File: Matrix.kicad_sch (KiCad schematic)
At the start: 2 parts

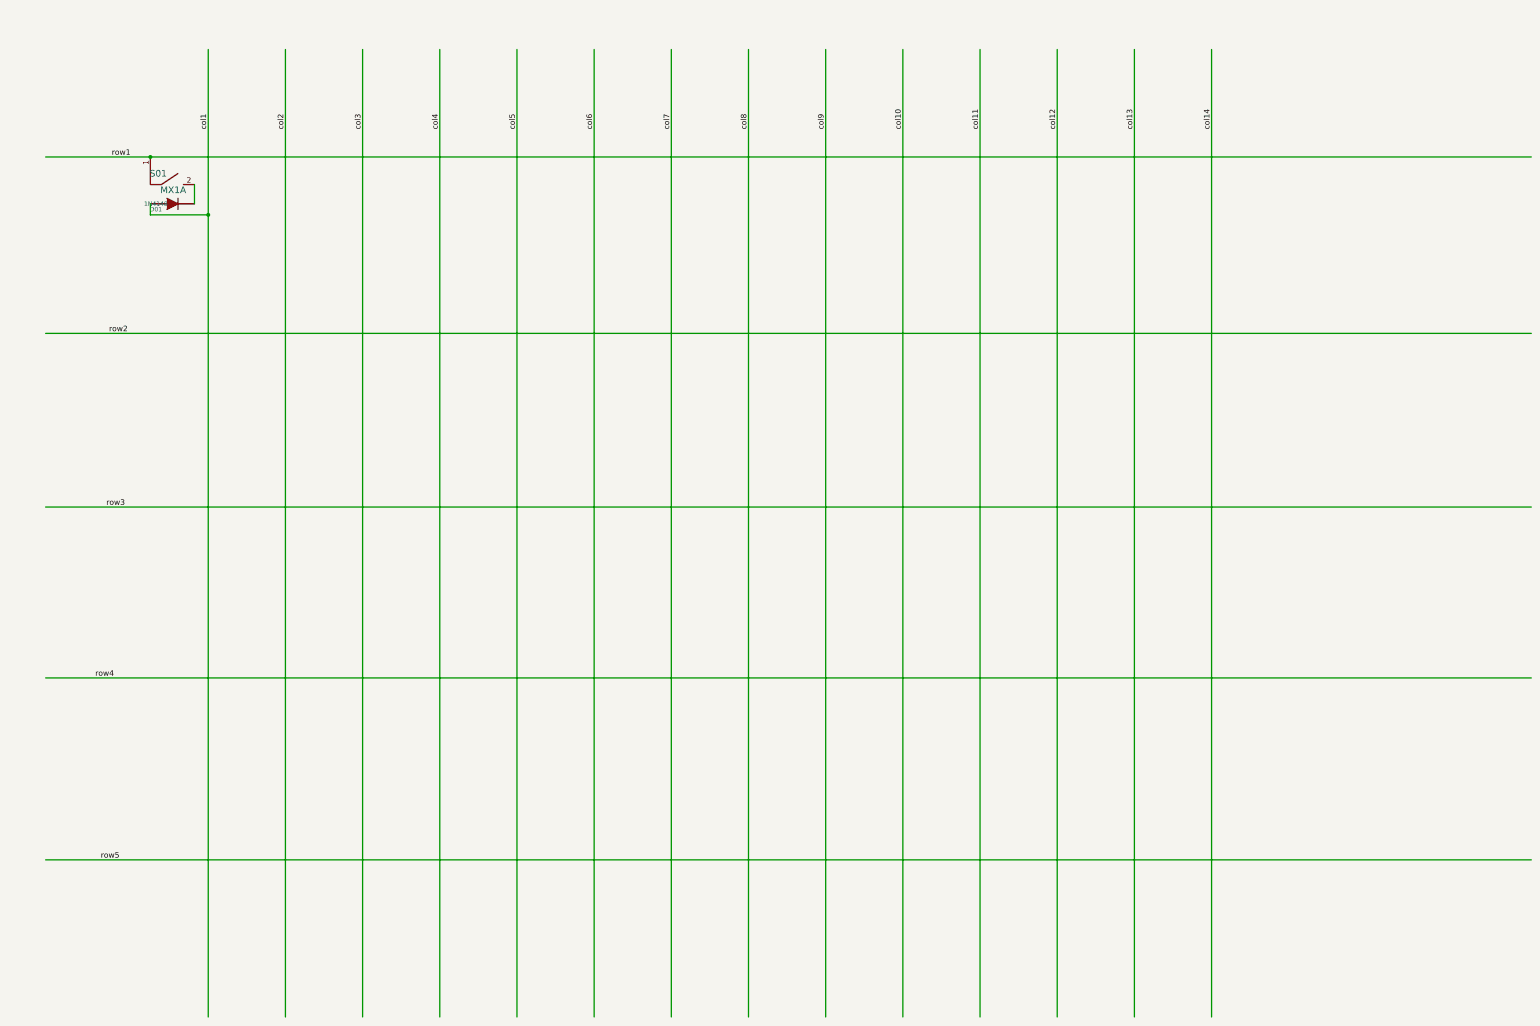
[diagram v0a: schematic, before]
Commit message: Fixed column and row labels on Matrix
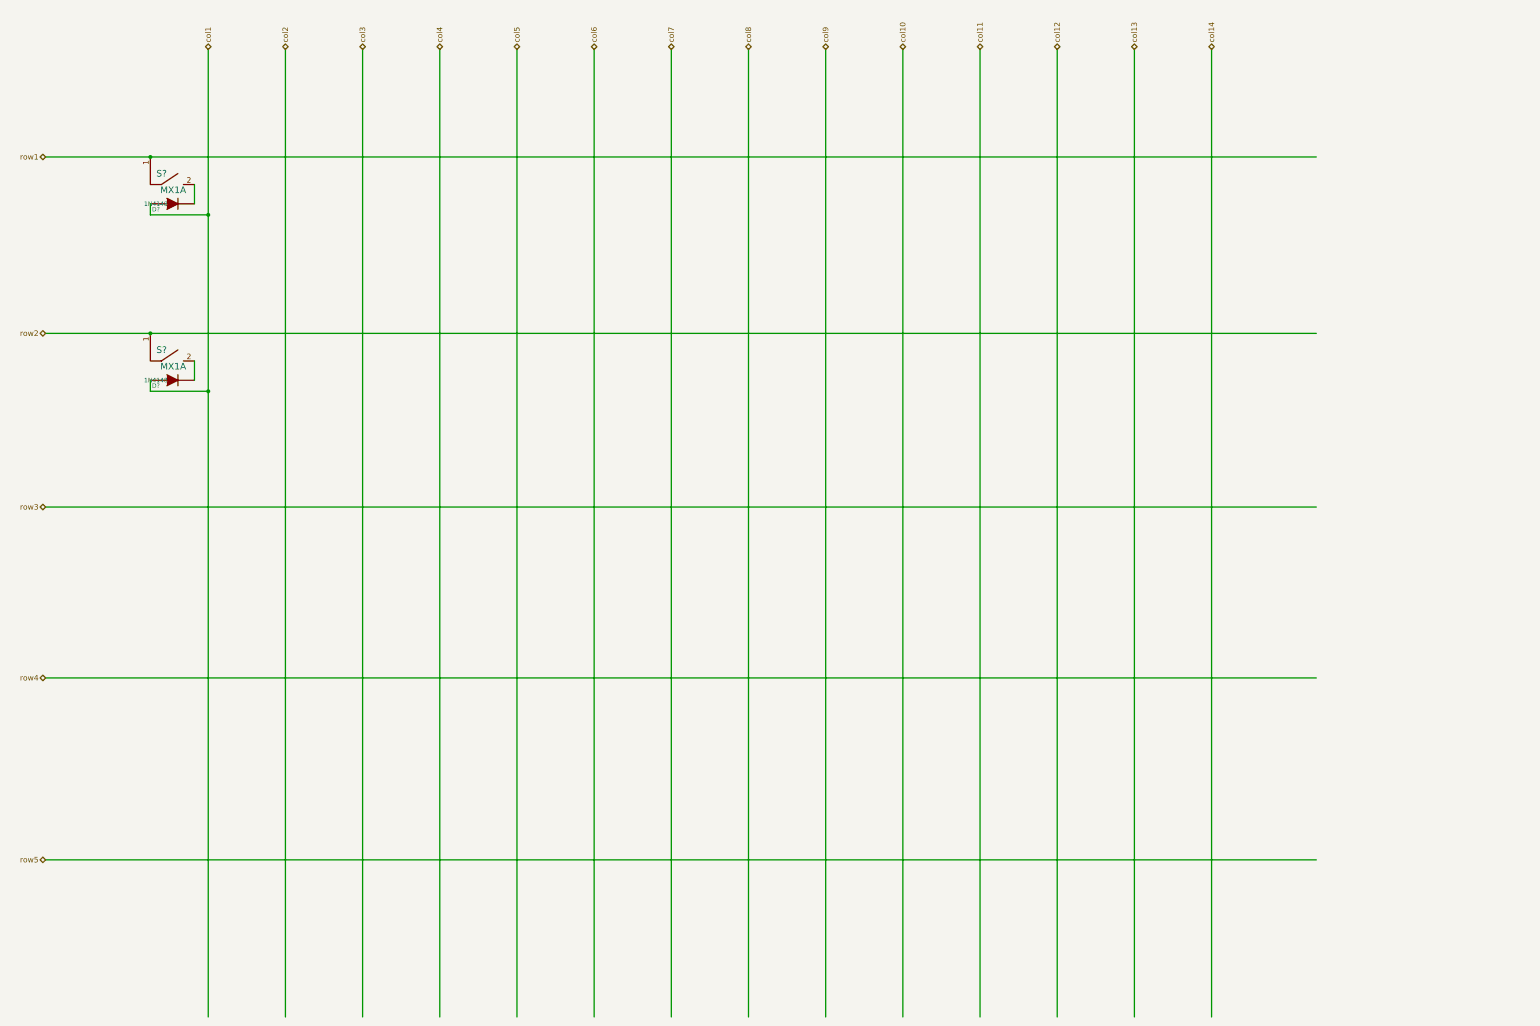
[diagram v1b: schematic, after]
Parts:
- added D?: 1N4148, symbol device:DIODE
- added S?: MX1A, symbol mx1a-simple:MX1A
- renumbered D01 to D?, S01 to S?
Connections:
- net col1: now also D?.1 (A)
- net row2: now also S?.1
- new net: D?.2 (K), S?.2
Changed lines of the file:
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@@
   (junction (at 69.85 63.5) (diameter 0) (color 0 0 0 0)
   )
+  (junction (at 56.515 90.805) (diameter 0) (color 0 0 0 0)
+  )
   (junction (at 56.515 50.165) (diameter 0) (color 0 0 0 0)
   )
+  (junction (at 69.85 104.14) (diameter 0) (color 0 0 0 0)
+  )
   (wire (pts (xy 158.75 25.4) (xy 158.75 248.285))
     (stroke (width 0) (type default) (color 0 0 0 0))
@@
     (stroke (width 0) (type default) (color 0 0 0 0))
   )
+  (wire (pts (xy 56.515 90.805) (xy 325.12 90.805))
+    (stroke (width 0) (type default) (color 0 0 0 0))
+  )
   (wire (pts (xy 247.65 25.4) (xy 247.65 248.285))
     (stroke (width 0) (type default) (color 0 0 0 0))
@@
     (stroke (width 0) (type default) (color 0 0 0 0))
   )
-  (wire (pts (xy 32.385 90.805) (xy 374.65 90.805))
+  (wire (pts (xy 56.515 104.14) (xy 69.85 104.14))
+    (stroke (width 0) (type default) (color 0 0 0 0))
+  )
+  (wire (pts (xy 69.85 104.14) (xy 69.85 248.285))
+    (stroke (width 0) (type default) (color 0 0 0 0))
+  )
+  (wire (pts (xy 66.675 97.155) (xy 66.675 101.6))
+    (stroke (width 0) (type default) (color 0 0 0 0))
+  )
+  (wire (pts (xy 32.385 90.805) (xy 56.515 90.805))
     (stroke (width 0) (type default) (color 0 0 0 0))
   )
@@
     (stroke (width 0) (type default) (color 0 0 0 0))
   )
-  (wire (pts (xy 32.385 170.18) (xy 374.65 170.18))
+  (wire (pts (xy 32.385 170.18) (xy 325.12 170.18))
     (stroke (width 0) (type default) (color 0 0 0 0))
   )
@@
     (stroke (width 0) (type default) (color 0 0 0 0))
   )
-  (wire (pts (xy 69.85 63.5) (xy 69.85 248.285))
-    (stroke (width 0) (type default) (color 0 0 0 0))
-  )
-  (wire (pts (xy 32.385 212.09) (xy 374.65 212.09))
+  (wire (pts (xy 69.85 63.5) (xy 69.85 104.14))
+    (stroke (width 0) (type default) (color 0 0 0 0))
+  )
+  (wire (pts (xy 32.385 212.09) (xy 325.12 212.09))
+    (stroke (width 0) (type default) (color 0 0 0 0))
+  )
+  (wire (pts (xy 56.515 101.6) (xy 56.515 104.14))
     (stroke (width 0) (type default) (color 0 0 0 0))
   )
@@
     (stroke (width 0) (type default) (color 0 0 0 0))
   )
-  (wire (pts (xy 32.385 130.81) (xy 374.65 130.81))
+  (wire (pts (xy 32.385 130.81) (xy 325.12 130.81))
     (stroke (width 0) (type default) (color 0 0 0 0))
   )
@@
     (stroke (width 0) (type default) (color 0 0 0 0))
   )
-  (wire (pts (xy 56.515 50.165) (xy 374.65 50.165))
-    (stroke (width 0) (type default) (color 0 0 0 0))
-  )
-  (label "col14" (at 300.99 43.815 90)
-    (effects (font (size 1.27 1.27)) (justify left bottom))
-  )
-  (label "col11" (at 247.65 43.815 90)
-    (effects (font (size 1.27 1.27)) (justify left bottom))
-  )
-  (label "col2" (at 87.63 43.815 90)
-    (effects (font (size 1.27 1.27)) (justify left bottom))
-  )
-  (label "row1" (at 47.625 50.165 0)
-    (effects (font (size 1.27 1.27)) (justify left bottom))
-  )
-  (label "row4" (at 43.815 170.18 0)
-    (effects (font (size 1.27 1.27)) (justify left bottom))
-  )
-  (label "col13" (at 283.21 43.815 90)
-    (effects (font (size 1.27 1.27)) (justify left bottom))
-  )
-  (label "col1" (at 69.85 43.815 90)
-    (effects (font (size 1.27 1.27)) (justify left bottom))
-  )
-  (label "col7" (at 176.53 43.815 90)
-    (effects (font (size 1.27 1.27)) (justify left bottom))
-  )
-  (label "col6" (at 158.75 43.815 90)
-    (effects (font (size 1.27 1.27)) (justify left bottom))
-  )
-  (label "row5" (at 45.085 212.09 0)
-    (effects (font (size 1.27 1.27)) (justify left bottom))
-  )
-  (label "row2" (at 46.99 90.805 0)
-    (effects (font (size 1.27 1.27)) (justify left bottom))
-  )
-  (label "col12" (at 265.43 43.815 90)
-    (effects (font (size 1.27 1.27)) (justify left bottom))
-  )
-  (label "col5" (at 140.97 43.815 90)
-    (effects (font (size 1.27 1.27)) (justify left bottom))
-  )
-  (label "col9" (at 212.09 43.815 90)
-    (effects (font (size 1.27 1.27)) (justify left bottom))
-  )
-  (label "col4" (at 123.19 43.815 90)
-    (effects (font (size 1.27 1.27)) (justify left bottom))
-  )
-  (label "col8" (at 194.31 43.815 90)
-    (effects (font (size 1.27 1.27)) (justify left bottom))
-  )
-  (label "row3" (at 46.355 130.81 0)
-    (effects (font (size 1.27 1.27)) (justify left bottom))
-  )
-  (label "col10" (at 229.87 43.815 90)
-    (effects (font (size 1.27 1.27)) (justify left bottom))
-  )
-  (label "col3" (at 105.41 43.815 90)
-    (effects (font (size 1.27 1.27)) (justify left bottom))
+  (wire (pts (xy 56.515 50.165) (xy 325.12 50.165))
+    (stroke (width 0) (type default) (color 0 0 0 0))
+  )
+  (hierarchical_label "col11" (shape tri_state) (at 247.65 25.4 90)
+    (effects (font (size 1.27 1.27)) (justify left))
+  )
+  (hierarchical_label "col4" (shape tri_state) (at 123.19 25.4 90)
+    (effects (font (size 1.27 1.27)) (justify left))
+  )
+  (hierarchical_label "col8" (shape tri_state) (at 194.31 25.4 90)
+    (effects (font (size 1.27 1.27)) (justify left))
+  )
+  (hierarchical_label "row4" (shape tri_state) (at 32.385 170.18 180)
+    (effects (font (size 1.27 1.27)) (justify right))
+  )
+  (hierarchical_label "col1" (shape tri_state) (at 69.85 25.4 90)
+    (effects (font (size 1.27 1.27)) (justify left))
+  )
+  (hierarchical_label "col2" (shape tri_state) (at 87.63 25.4 90)
+    (effects (font (size 1.27 1.27)) (justify left))
+  )
+  (hierarchical_label "row1" (shape tri_state) (at 32.385 50.165 180)
+    (effects (font (size 1.27 1.27)) (justify right))
+  )
+  (hierarchical_label "col10" (shape tri_state) (at 229.87 25.4 90)
+    (effects (font (size 1.27 1.27)) (justify left))
+  )
+  (hierarchical_label "col6" (shape tri_state) (at 158.75 25.4 90)
+    (effects (font (size 1.27 1.27)) (justify left))
+  )
+  (hierarchical_label "col3" (shape tri_state) (at 105.41 25.4 90)
+    (effects (font (size 1.27 1.27)) (justify left))
+  )
+  (hierarchical_label "row3" (shape tri_state) (at 32.385 130.81 180)
+    (effects (font (size 1.27 1.27)) (justify right))
+  )
+  (hierarchical_label "row2" (shape tri_state) (at 32.385 90.805 180)
+    (effects (font (size 1.27 1.27)) (justify right))
+  )
+  (hierarchical_label "col5" (shape tri_state) (at 140.97 25.4 90)
+    (effects (font (size 1.27 1.27)) (justify left))
+  )
+  (hierarchical_label "col12" (shape tri_state) (at 265.43 25.4 90)
+    (effects (font (size 1.27 1.27)) (justify left))
+  )
+  (hierarchical_label "col7" (shape tri_state) (at 176.53 25.4 90)
+    (effects (font (size 1.27 1.27)) (justify left))
+  )
+  (hierarchical_label "col9" (shape tri_state) (at 212.09 25.4 90)
+    (effects (font (size 1.27 1.27)) (justify left))
+  )
+  (hierarchical_label "row5" (shape tri_state) (at 32.385 212.09 180)
+    (effects (font (size 1.27 1.27)) (justify right))
+  )
+  (hierarchical_label "col14" (shape tri_state) (at 300.99 25.4 90)
+    (effects (font (size 1.27 1.27)) (justify left))
+  )
+  (hierarchical_label "col13" (shape tri_state) (at 283.21 25.4 90)
+    (effects (font (size 1.27 1.27)) (justify left))
   )
   (symbol (lib_id "mx1a-simple:MX1A") (at 61.595 60.325 0) (unit 1)
     (in_bom yes) (on_board yes)
-    (property "Reference" "S01" (id 0) (at 60.325 53.975 0)
+    (property "Reference" "S?" (id 0) (at 60.325 53.975 0)
       (effects (font (size 1.524 1.524)) (justify right))
     )
@@
     (pin "2")
   )
+  (symbol (lib_id "device:DIODE") (at 61.595 101.6 0) (unit 1)
+    (in_bom yes) (on_board yes)
+    (property "Reference" "D?" (id 0) (at 57.785 102.87 0)
+      (effects (font (size 1.016 1.016)))
+    )
+    (property "Value" "1N4148" (id 1) (at 57.785 101.6 0)
+      (effects (font (size 1.016 1.016)))
+    )
+    (property "Footprint" "" (id 2) (at 61.595 101.6 0)
+      (effects (font (size 1.27 1.27)) hide)
+    )
+    (property "Datasheet" "" (id 3) (at 61.595 101.6 0)
+      (effects (font (size 1.27 1.27)) hide)
+    )
+    (pin "1")
+    (pin "2")
+  )
   (symbol (lib_id "device:DIODE") (at 61.595 60.96 0) (unit 1)
     (in_bom yes) (on_board yes)
-    (property "Reference" "D01" (id 0) (at 57.785 62.23 0)
+    (property "Reference" "D?" (id 0) (at 57.785 62.23 0)
       (effects (font (size 1.016 1.016)))
     )
@@
       (effects (font (size 1.27 1.27)) hide)
     )
+    (pin "1")
+    (pin "2")
+  )
+  (symbol (lib_id "mx1a-simple:MX1A") (at 61.595 100.965 0) (unit 1)
+    (in_bom yes) (on_board yes)
+    (property "Reference" "S?" (id 0) (at 60.325 94.615 0)
+      (effects (font (size 1.524 1.524)) (justify right))
+    )
+    (property "Value" "MX1A" (id 1) (at 64.77 98.425 0)
+      (effects (font (size 1.524 1.524)) (justify right))
+    )
+    (property "Footprint" "" (id 2) (at 61.595 100.965 0)
+      (effects (font (size 1.27 1.27)) hide)
+    )
+    (property "Datasheet" "" (id 3) (at 61.595 100.965 0)
+      (effects (font (size 1.27 1.27)) hide)
+    )

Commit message: Added key labels signifiying where each key will go to the matrix
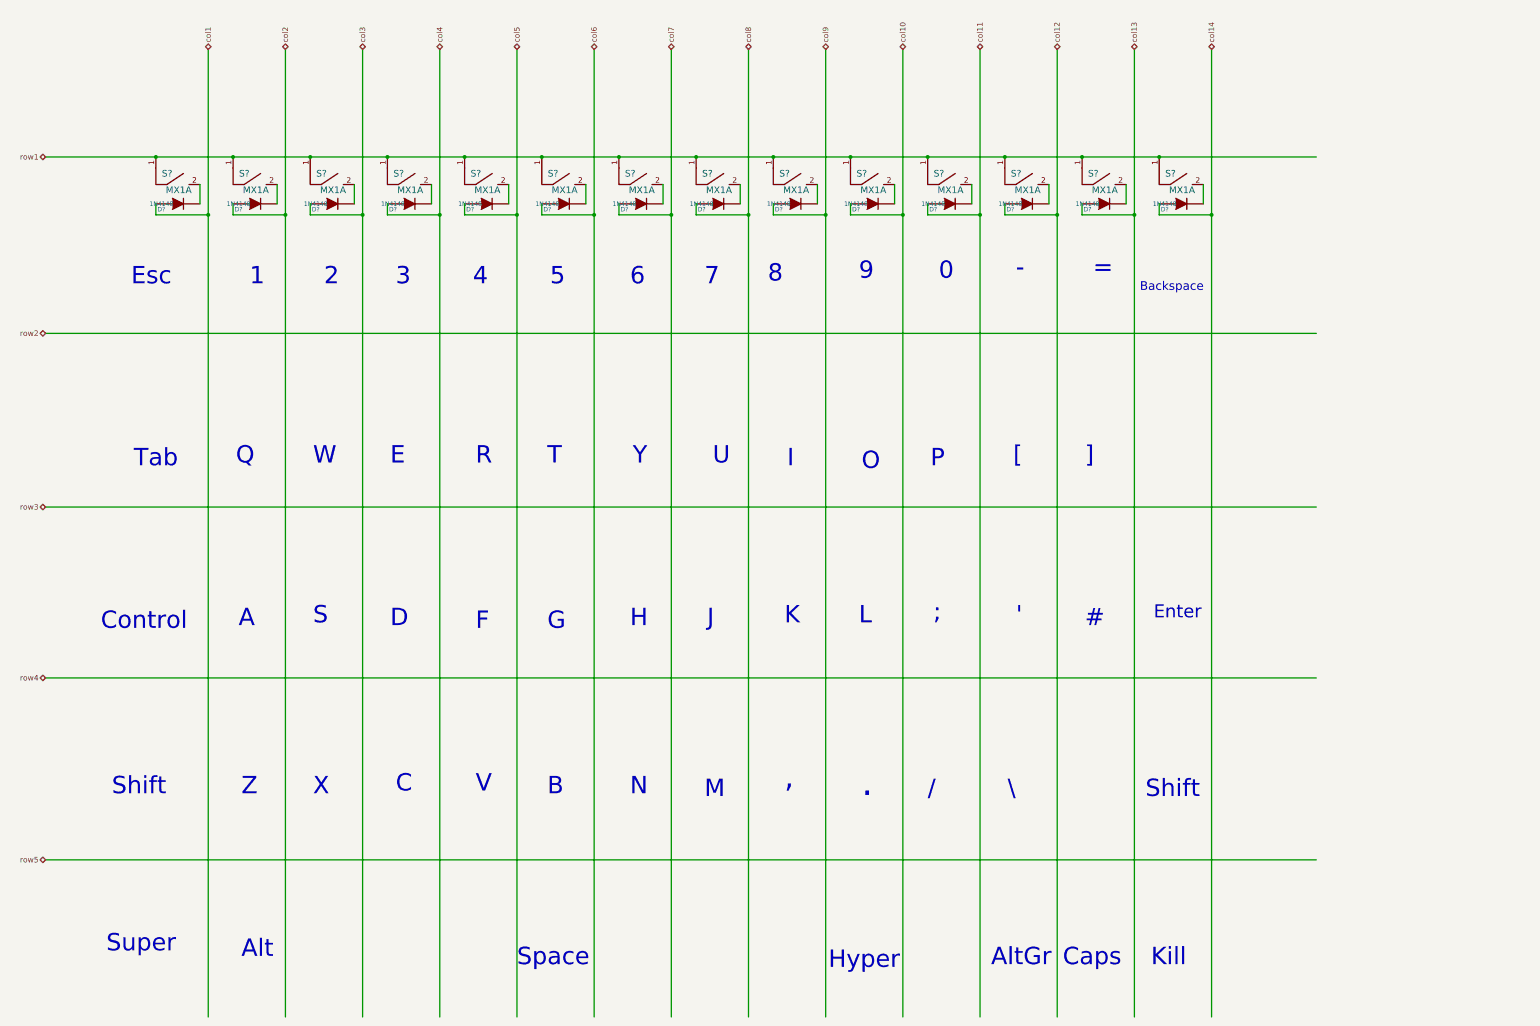
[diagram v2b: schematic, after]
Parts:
- removed D?: 1N4148, symbol device:DIODE
- removed S?: MX1A, symbol mx1a-simple:MX1A
- added D? (x13): 1N4148, symbol device:DIODE
- added S? (x13): MX1A, symbol mx1a-simple:MX1A
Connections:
- net col10: now also D?.1 (A)
- net col11: now also D?.1 (A)
- net col12: now also D?.1 (A)
- net col13: now also D?.1 (A)
- net col14: now also D?.1 (A)
- net col2: now also D?.1 (A)
- net col3: now also D?.1 (A)
- net col4: now also D?.1 (A)
- net col5: now also D?.1 (A)
- net col6: now also D?.1 (A)
- net col7: now also D?.1 (A)
- net col8: now also D?.1 (A)
- net col9: now also D?.1 (A)
- net row1: now also S?.1, S?.1, S?.1, S?.1, S?.1, S?.1, S?.1, S?.1, S?.1, S?.1, S?.1, S?.1, S?.1
- new net: D?.2 (K), S?.2 (x13)
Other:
- note added: "#"
- note added: "'"
- note added: ","
- note added: "-"
- note added: "."
- note added: "/"
- note added: "0"
- note added: "1"
- note added: "2"
- note added: "3"
- note added: "4"
- note added: "5"
- note added: "6"
- note added: "7"
- note added: "8"
- note added: "9"
- note added: ";"
- note added: "="
- note added: "A"
- note added: "Alt"
- note added: "AltGr"
- note added: "B"
- note added: "Backspace"
- note added: "C"
- note added: "Caps"
- note added: "Control"
- note added: "D"
- note added: "E"
- note added: "Enter"
- note added: "Esc"
- note added: "F"
- note added: "G"
- note added: "H"
- note added: "Hyper"
- note added: "I"
- note added: "J"
- note added: "K"
- note added: "Kill"
- note added: "L"
- note added: "M"
- note added: "N"
- note added: "O"
- note added: "P"
- note added: "Q"
- note added: "R"
- note added: "S"
- note added: "Shift"
- note added: "Space"
- note added: "Super"
- note added: "T"
- note added: "Tab"
- note added: "U"
- note added: "V"
- note added: "W"
- note added: "X"
- note added: "Y"
- note added: "Z"
- note added: "["
- note added: "\"
- note added: "]"
- moved on the sheet: D?, S?
